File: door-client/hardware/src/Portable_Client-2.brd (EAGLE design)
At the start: 48.9 x 36.8 mm, 34 parts, among them IC3 MC78M05ABT, U1 ATMEGA328P-AU, Y1 12MHZ

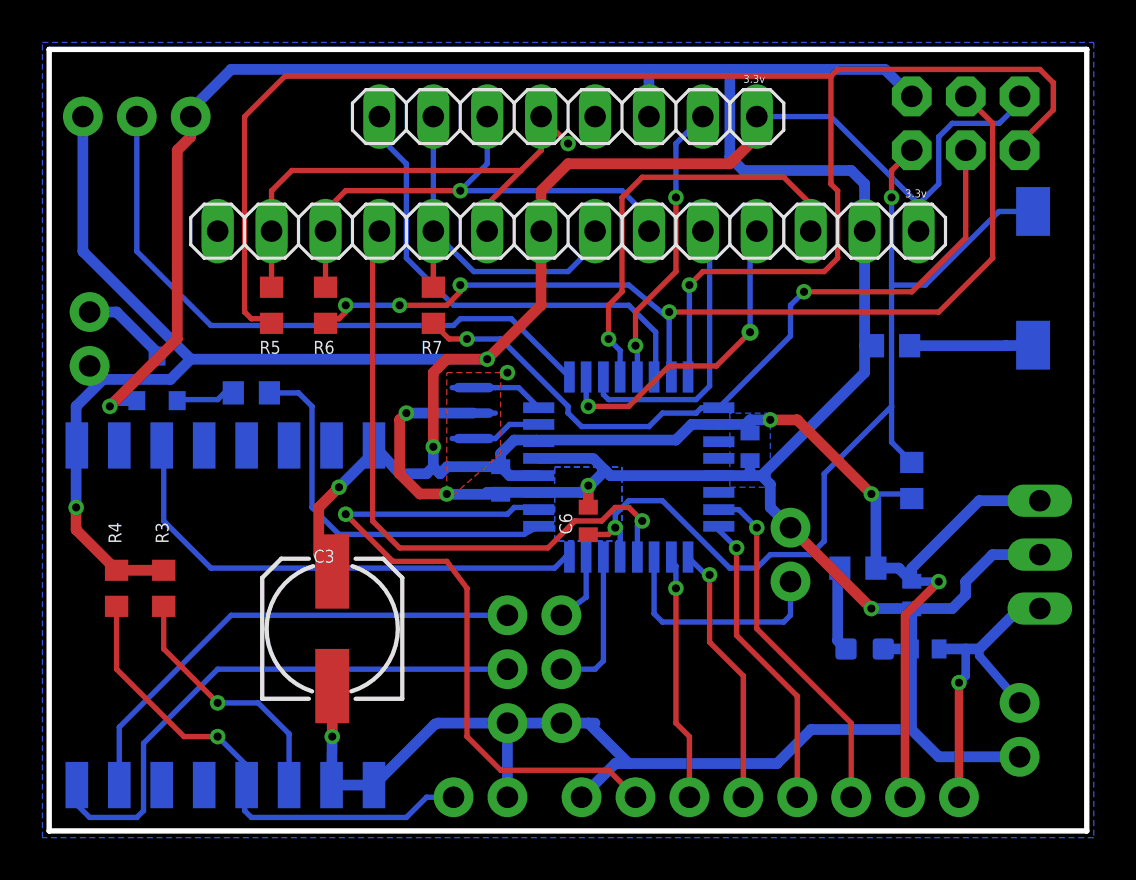
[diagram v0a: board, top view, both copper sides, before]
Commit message: re-route swapped pins on board
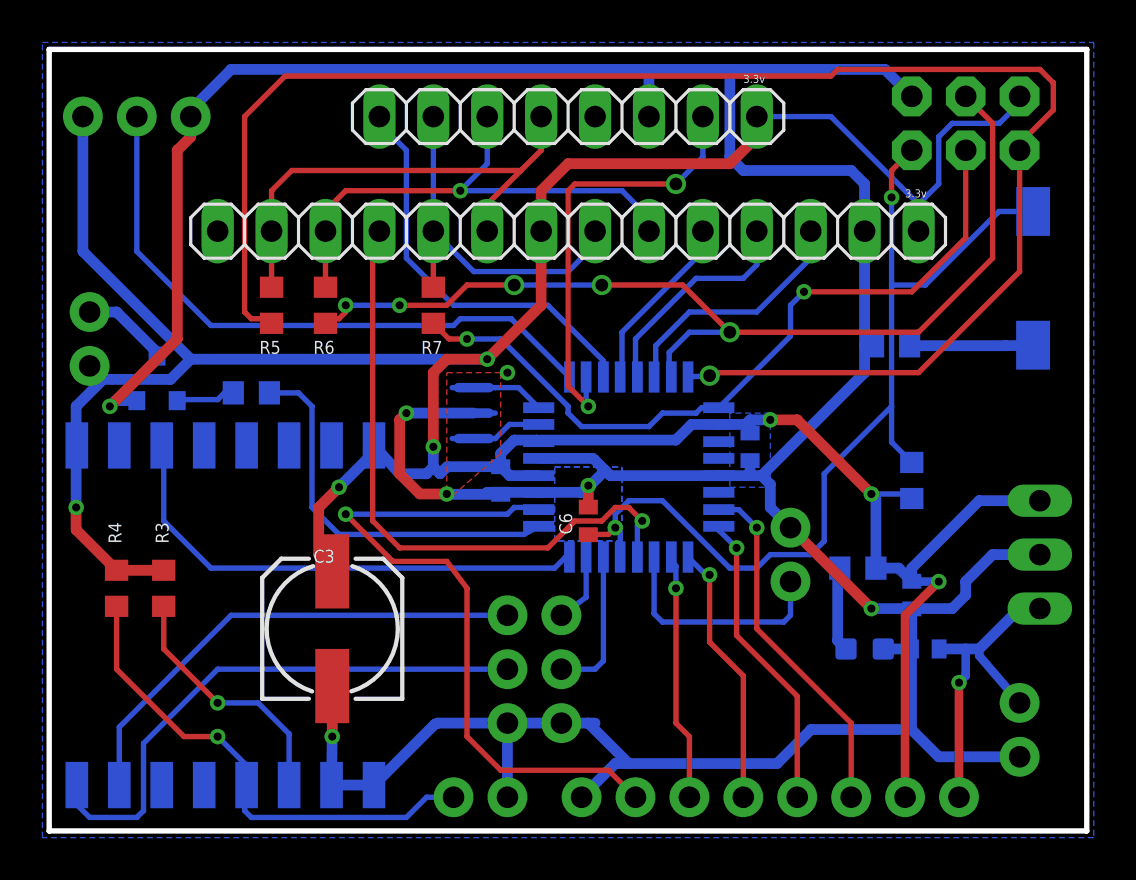
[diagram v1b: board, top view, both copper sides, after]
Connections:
- net D10: now also LCD/TOUCH.12; no longer NFC.8
- net D6: now also NFC.2; no longer LCD/TOUCH.11
- net D7: now also NFC.8; no longer LCD/TOUCH.10
- net D8: now also LCD/TOUCH.10; no longer LCD/TOUCH.12
- net D9: now also LCD/TOUCH.11; no longer NFC.2
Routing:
- net D8: track 20.0 -> 8.49 mm, vias 1 -> 0
- net D10: track 22.5 -> 11.8 mm
- net D7: track 13.8 -> 19.4 mm
- net D6: track 15.4 -> 20.9 mm
- net D9: track 13.6 -> 10.6 mm, vias 2 -> 0
- net D12: track 74.4 -> 77.1 mm
- net D11: track 45.4 -> 47.3 mm, vias 4 -> 5
- net MISO: track 24.9 -> 23.1 mm, vias 1 -> 0

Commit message: re-route sections to shorten traces and reduce number of vias
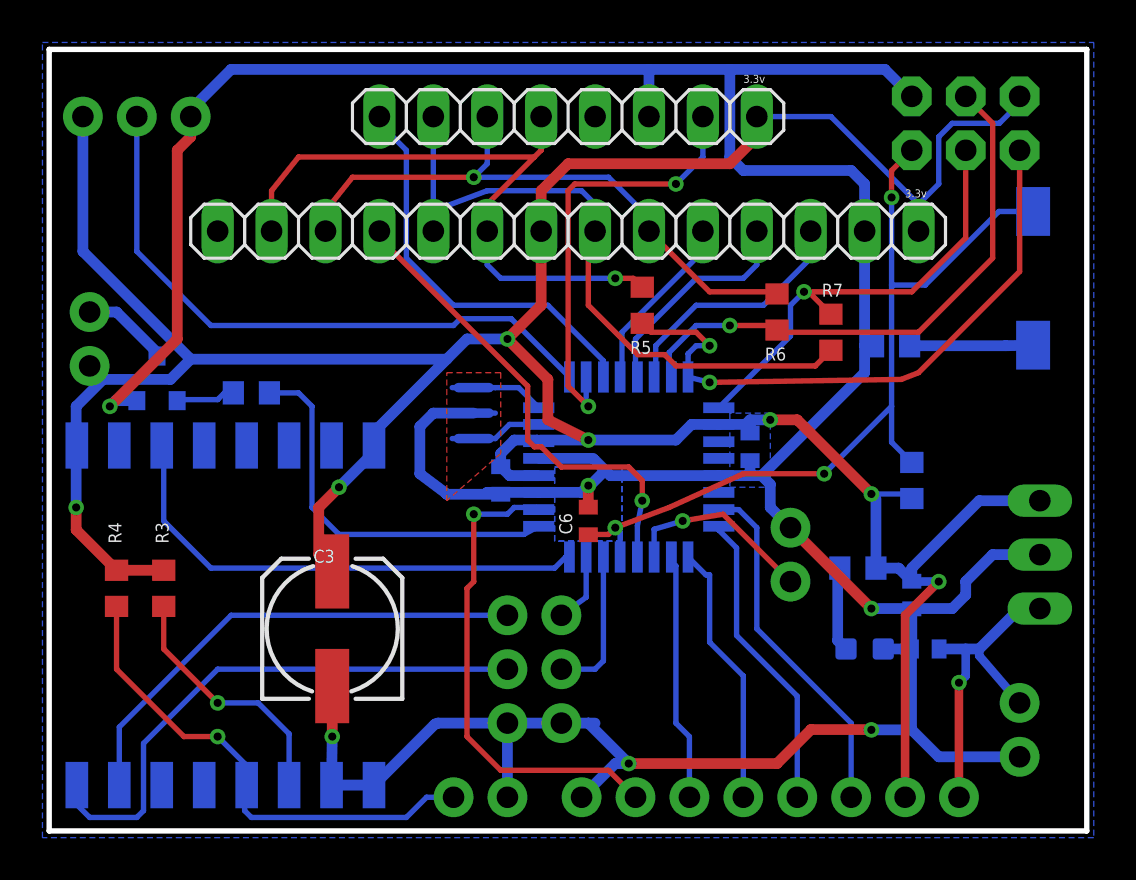
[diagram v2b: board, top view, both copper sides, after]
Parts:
- moved R6 21.3 mm to (34.3, 33.3)
- moved R7 18.8 mm to (36.8, 32.4), turned to 270 degrees
- moved R5 17.5 mm to (27.9, 33.7)
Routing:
- net D12: track 77.1 -> 29.6 mm, vias 1 -> 2
- net D11: track 47.3 -> 26.7 mm, vias 5 -> 1
- net D13: track 36.7 -> 21.9 mm, vias 2 -> 1
- net SCK: track 17.6 -> 32.2 mm
- net D4: track 32.6 -> 23.0 mm
- net MISO: track 23.1 -> 30.8 mm, vias 0 -> 1
- net D19: track 29.9 -> 23.0 mm
- net RESET: track 47.5 -> 42.1 mm, vias 2 -> 3
- net MOSI: track 24.4 -> 28.8 mm
- net GND: track 184.0 -> 181.9 mm
- net 3V3: track 157.8 -> 155.8 mm
- net D18: track 11.0 -> 9.13 mm, vias 0 -> 1
- net D17: vias 1 -> 0
- net D16: vias 1 -> 0
- net D15: vias 1 -> 0
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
